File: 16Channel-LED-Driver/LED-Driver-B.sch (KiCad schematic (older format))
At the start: 42 parts, among them P9 CONN_01X08, Q51 BC413, Q52 BC413, Q55 BC413, Q56 BUT11, Q57 BC413, Q58 BUT11, Q59 BC413, Q60 BC413, Q63 BC413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

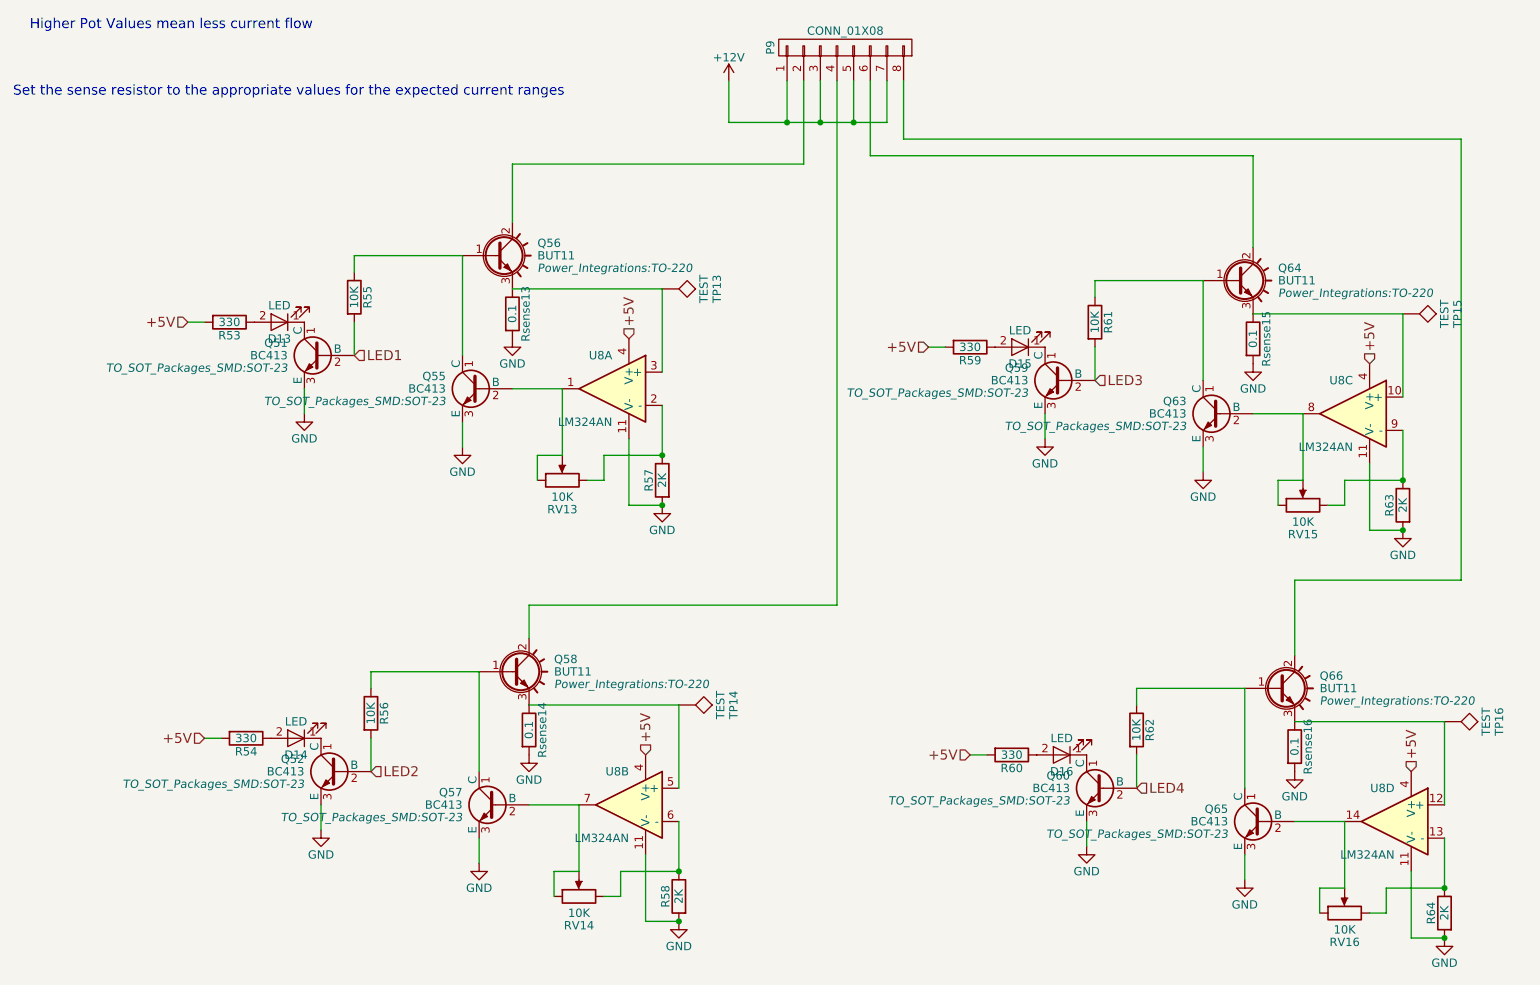
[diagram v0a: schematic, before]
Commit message: Did Revision B of the 16 Channel board, also exported some gerbers
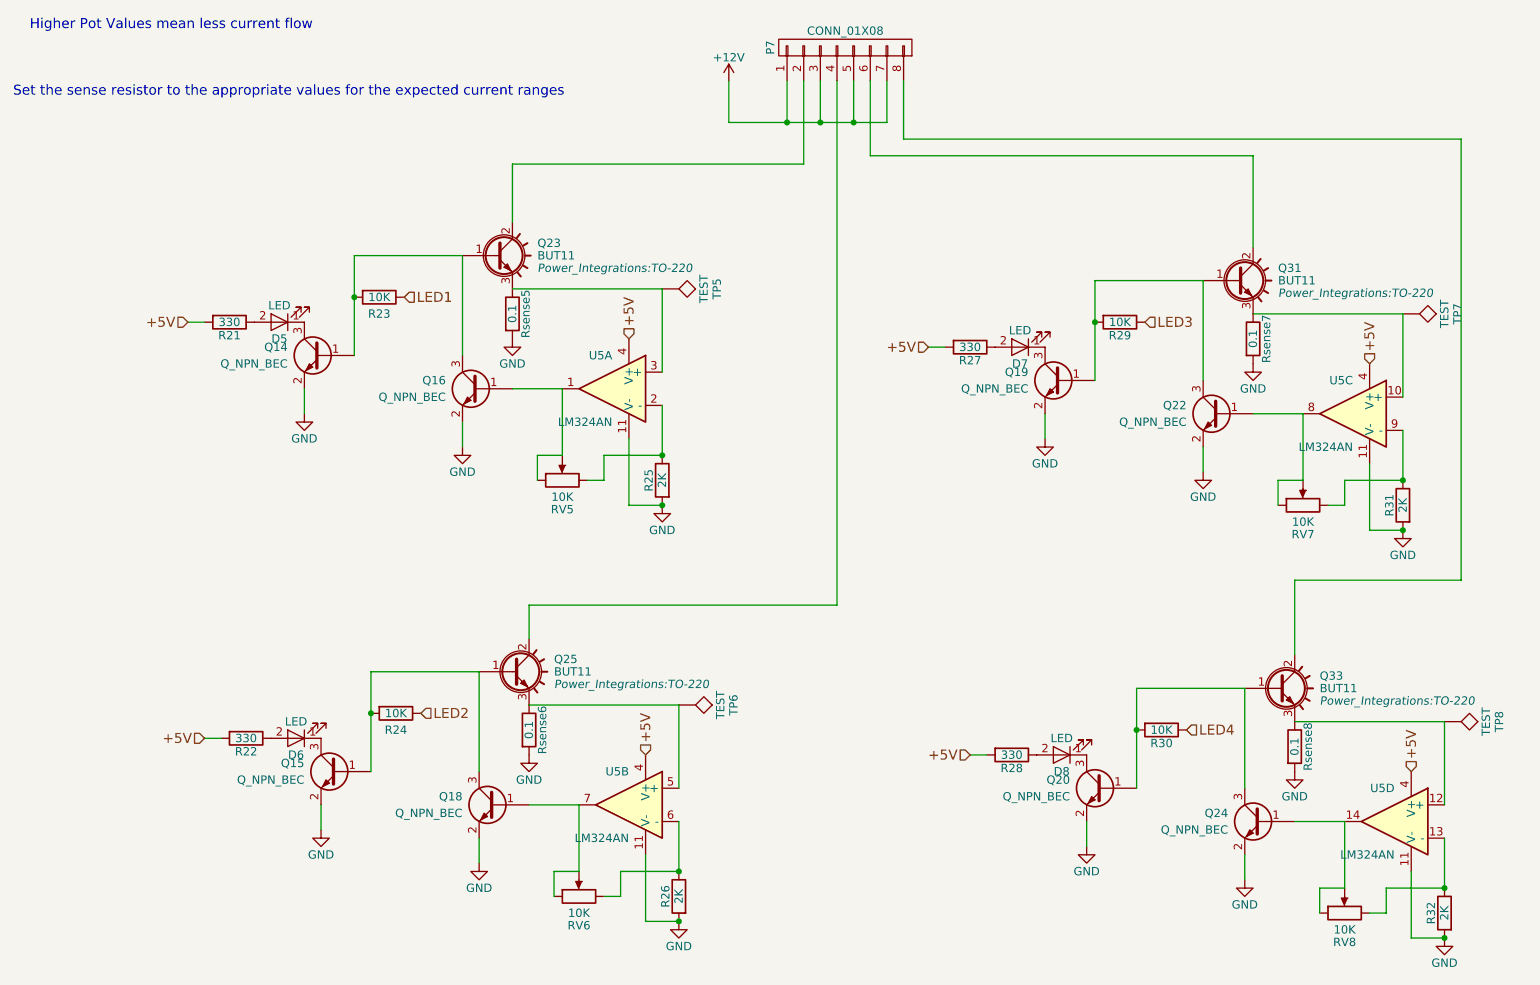
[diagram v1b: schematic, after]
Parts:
- removed Q51, Q52, Q55, Q57, Q59, Q60, Q63, Q65: BC413, TO_SOT_Packages_SMD:SOT-23, symbol BC413
- added Q14, Q15, Q16, Q18, Q19, Q20, Q22, Q24: Q_NPN_BEC, TO_SOT_Packages_SMD:SOT-23, symbol Q_NPN_BEC
- Rsense13, Rsense14, Rsense15, Rsense16: footprint Custom_Footprints:Current_Sense_Resistor -> Resistors_SMD:R_1206_HandSoldering
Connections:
- net GND: now also Q14.2 (E), Q15.2 (E), Q16.2 (E), Q18.2 (E), Q19.2 (E), Q20.2 (E), Q22.2 (E), Q24.2 (E)
- net LED1: now also R55.1; no longer R55.2
- net LED2: now also R56.1; no longer R56.2
- net LED3: now also R61.1; no longer R61.2
- net LED4: now also R62.1; no longer R62.2
- net at Q56.1 (B): now also R55.2, Q14.1 (B), Q16.3 (C); no longer R55.1
- net at RV13.1, RV13.2, U8.1: now also Q16.1 (B)
- net at D13.1 (K): now also Q14.3 (C)
- net at D15.1 (K): now also Q19.3 (C)
- net at Q58.1 (B): now also R56.2, Q15.1 (B), Q18.3 (C); no longer R56.1
- net at RV14.1, RV14.2, U8.7: now also Q18.1 (B)
- net at D14.1 (K): now also Q15.3 (C)
- net at RV16.1, RV16.2, U8.14: now also Q24.1 (B)
- net at Q66.1 (B): now also R62.2, Q20.1 (B), Q24.3 (C); no longer R62.1
- net at D16.1 (K): now also Q20.3 (C)
- net at RV15.1, RV15.2, U8.8: now also Q22.1 (B)
- net at Q64.1 (B): now also R61.2, Q19.1 (B), Q22.3 (C); no longer R61.1
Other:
- moved on the sheet: R23, R24, R29, R30

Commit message: Did third and hopefully final revision of the 16 channel LED board. I like making dumb mistakes. :(
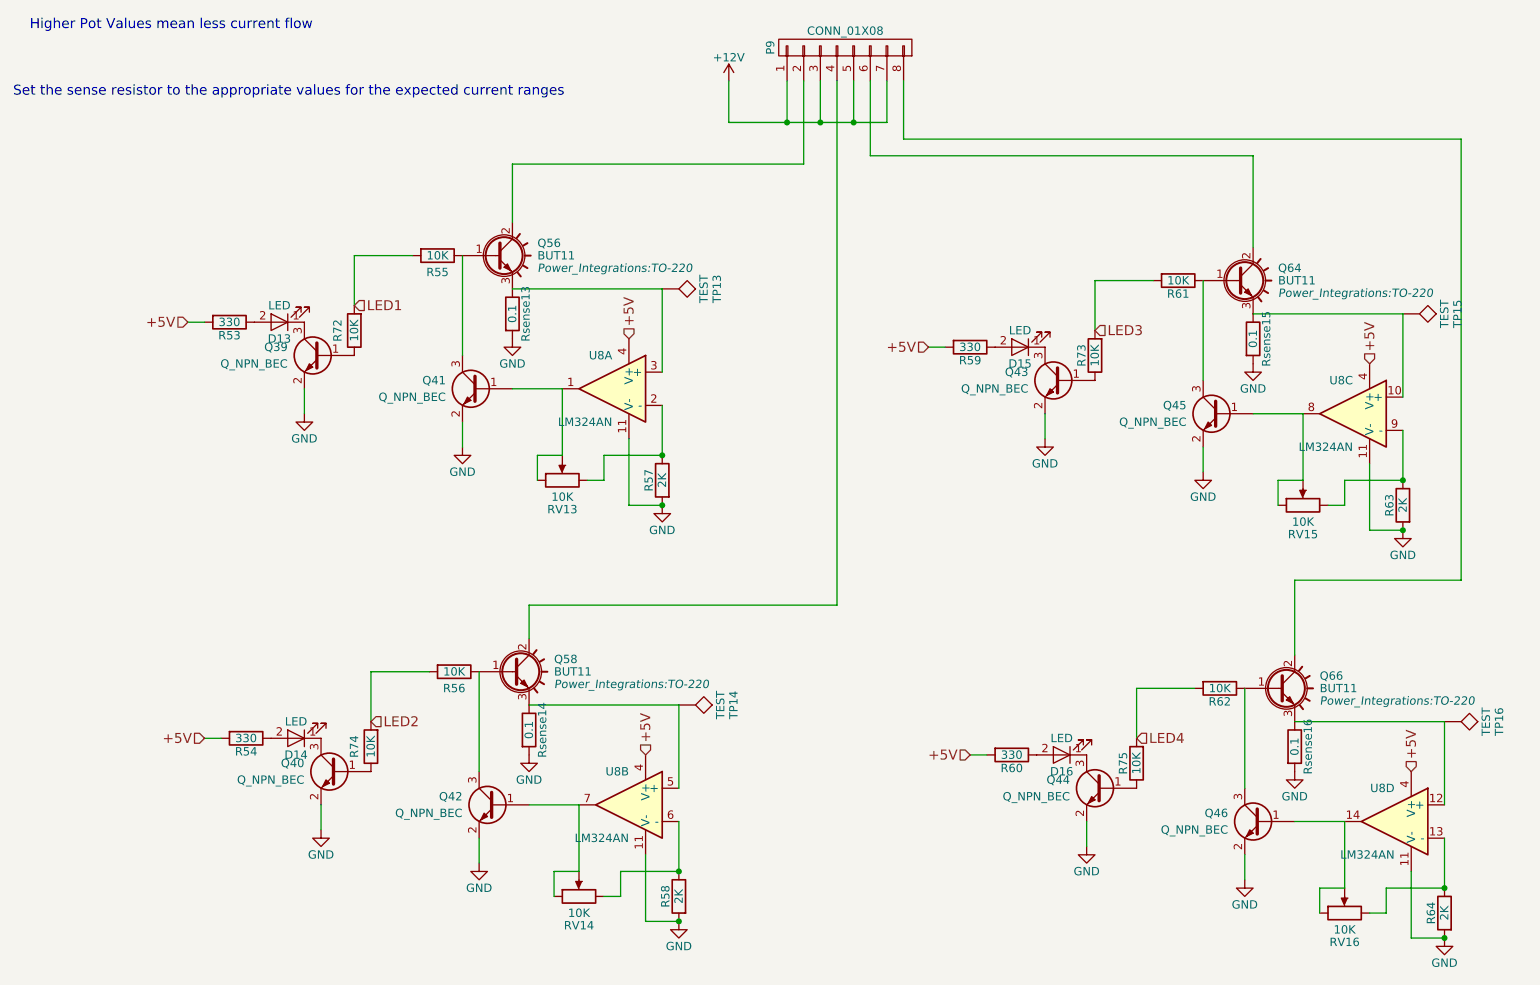
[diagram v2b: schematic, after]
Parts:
- added R68, R69, R70, R71: 10K, Resistors_SMD:R_0805_HandSoldering, symbol R
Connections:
- net LED1: now also R55.2, R68.2; no longer R55.1
- net LED2: now also R56.2, R70.2; no longer R56.1
- net LED3: now also R61.2, R69.2; no longer R61.1
- net LED4: now also R62.2, R71.2; no longer R62.1
- net at Q16.3 (C), Q56.1 (B): now also R55.1; no longer Q14.1 (B), R55.2
- net at Q18.3 (C), Q58.1 (B): now also R56.1; no longer Q15.1 (B), R56.2
- net at Q24.3 (C), Q66.1 (B): now also R62.1; no longer Q20.1 (B), R62.2
- net at Q22.3 (C), Q64.1 (B): now also R61.1; no longer Q19.1 (B), R61.2
- new net: Q14.1 (B), R68.1
- new net: Q15.1 (B), R70.1
- new net: Q20.1 (B), R71.1
- new net: Q19.1 (B), R69.1
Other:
- moved on the sheet: R55, R56, R61, R62

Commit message: Rev D of the 16 Channel board. Fixed an issue with the opamp driving BJTs
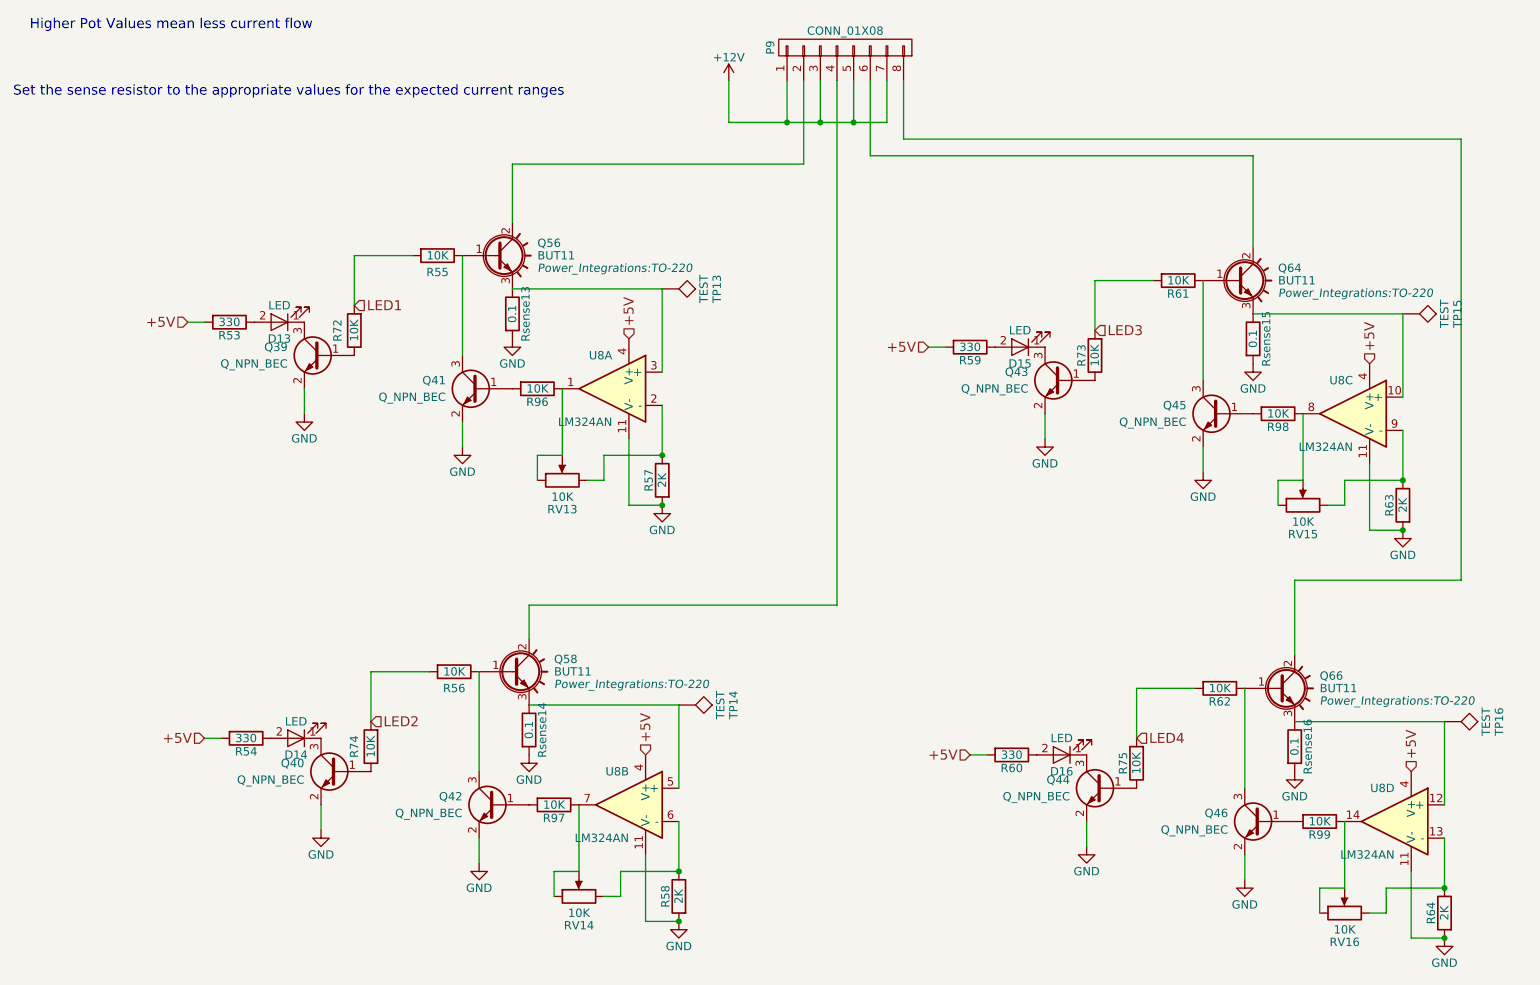
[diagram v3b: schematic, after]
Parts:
- added R88, R89, R90, R91: 10K, Resistors_SMD:R_0805_HandSoldering, symbol R
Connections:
- net at RV13.1, RV13.2, U8.1: now also R88.1; no longer Q16.1 (B)
- net at RV16.1, RV16.2, U8.14: now also R91.1; no longer Q24.1 (B)
- net at RV15.1, RV15.2, U8.8: now also R90.1; no longer Q22.1 (B)
- net at RV14.1, RV14.2, U8.7: now also R89.1; no longer Q18.1 (B)
- new net: Q16.1 (B), R88.2
- new net: Q18.1 (B), R89.2
- new net: Q24.1 (B), R91.2
- new net: Q22.1 (B), R90.2
